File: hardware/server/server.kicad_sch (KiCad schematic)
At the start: 12 parts

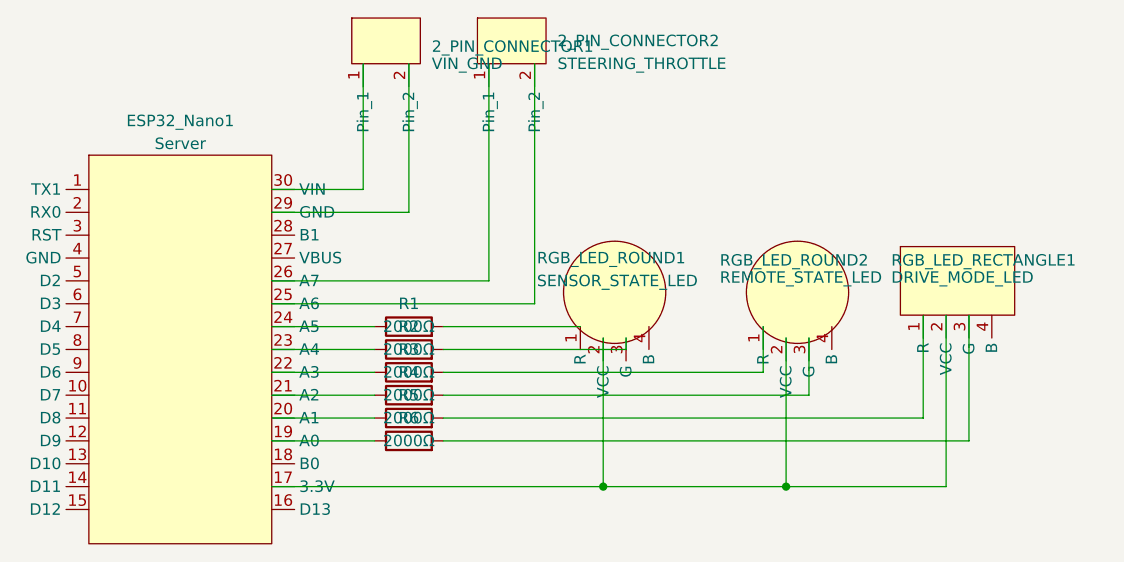
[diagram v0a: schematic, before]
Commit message: hardware: Add more footprint measurement.
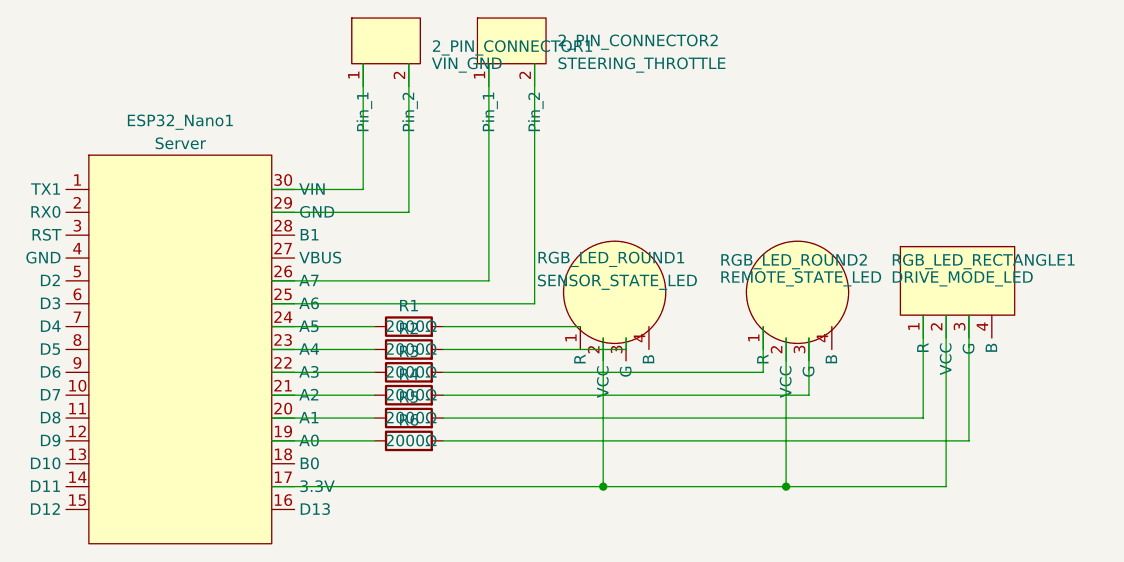
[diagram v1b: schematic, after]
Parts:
- removed R1, R2, R3, R4, R5, R6: 2000Ω, Autocam:Simple Resistor, symbol Device:R
- added R1, R2, R3, R4, R5, R6: 2000Ω, Autocam:Simple Resistor, symbol Autocam:Simple Resistor
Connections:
- net at RGB_LED_ROUND1.1 (R): now also R1.2
- net at RGB_LED_ROUND1.3 (G): now also R2.2
- net at ESP32_Nano1.23 (A4): now also R2.1
- net at ESP32_Nano1.21 (A2): now also R4.1
- net at RGB_LED_ROUND2.3 (G): now also R4.2
- net at ESP32_Nano1.19 (A0): now also R6.1
- net at ESP32_Nano1.20 (A1): now also R5.1
- net at ESP32_Nano1.22 (A3): now also R3.1
- net at ESP32_Nano1.24 (A5): now also R1.1
- net at RGB_LED_ROUND2.1 (R): now also R3.2
- net at RGB_LED_RECTANGLE1.1 (R): now also R5.2
- net at RGB_LED_RECTANGLE1.3 (G): now also R6.2

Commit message: hardware: Add remote PCB.
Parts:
- RGB_LED_RECTANGLE1: value DRIVE_MODE_LED -> DRIVE MODE
- RGB_LED_ROUND1: value SENSOR_STATE_LED -> SENSOR
- RGB_LED_ROUND2: value REMOTE_STATE_LED -> REMOTE
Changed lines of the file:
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@@
 			)
 		)
-		(property "Value" "SENSOR_STATE_LED"
+		(property "Value" "SENSOR"
 			(at 157.734 96.52 0)
 			(effects
@@
 			)
 		)
-		(property "Value" "REMOTE_STATE_LED"
+		(property "Value" "REMOTE"
 			(at 178.054 96.1391 0)
 			(effects
@@
 			)
 		)
-		(property "Value" "DRIVE_MODE_LED"
+		(property "Value" "DRIVE MODE"
 			(at 197.104 96.1391 0)
 			(effects

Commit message: hardware/server: Update LED shape, change to all round LEDs.
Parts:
- removed RGB_LED_RECTANGLE1: DRIVE MODE, Autocam:Anode RGB LED (Rectangle), symbol Autocam:ANODE_RGB_LED_Rectangle
- added RGB_LED_ROUND3: DRIVE_MODE, Autocam:Anode RGB LED (Round), symbol Autocam:ANODE_RGB_LED_Round
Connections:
- net at ESP32_Nano1.17 (3.3V), RGB_LED_ROUND1.2 (VCC), RGB_LED_ROUND2.2 (VCC): now also RGB_LED_ROUND3.2 (VCC)
- net at R6.2: now also RGB_LED_ROUND3.3 (G)
- net at R5.2: now also RGB_LED_ROUND3.1 (R)
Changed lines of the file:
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@@
 	(wire
 		(pts
-			(xy 185.42 119.38) (xy 203.2 119.38)
+			(xy 185.42 119.38) (xy 205.74 119.38)
 		)
 		(stroke
@@
 	(wire
 		(pts
-			(xy 147.32 111.76) (xy 200.66 111.76)
+			(xy 147.32 111.76) (xy 203.2 111.76)
 		)
 		(stroke
@@
 	(wire
 		(pts
-			(xy 205.74 100.33) (xy 205.74 114.3)
+			(xy 208.28 102.87) (xy 208.28 114.3)
 		)
 		(stroke
@@
 	(wire
 		(pts
-			(xy 205.74 114.3) (xy 147.32 114.3)
+			(xy 208.28 114.3) (xy 147.32 114.3)
 		)
 		(stroke
@@
 	(wire
 		(pts
-			(xy 203.2 100.33) (xy 203.2 119.38)
+			(xy 205.74 102.87) (xy 205.74 119.38)
 		)
 		(stroke
@@
 	(wire
 		(pts
-			(xy 200.66 111.76) (xy 200.66 100.33)
+			(xy 203.2 101.6) (xy 203.2 111.76)
 		)
 		(stroke
@@
 	)
 	(symbol
-		(lib_id "Autocam:ANODE_RGB_LED_Rectangle")
-		(at 204.47 97.79 0)
-		(unit 1)
-		(exclude_from_sim no)
-		(in_bom yes)
-		(on_board yes)
-		(dnp no)
-		(property "Reference" "RGB_LED_RECTANGLE1"
-			(at 197.104 94.234 0)
-			(effects
-				(font
-					(size 1.27 1.27)
-				)
-				(justify left)
-			)
-		)
-		(property "Value" "DRIVE MODE"
-			(at 197.104 96.1391 0)
-			(effects
-				(font
-					(size 1.27 1.27)
-				)
-				(justify left)
-			)
-		)
-		(property "Footprint" "Autocam:Anode RGB LED (Rectangle)"
-			(at 195.58 101.6 0)
-			(effects
-				(font
-					(size 1.27 1.27)
-				)
-				(hide yes)
-			)
-		)
-		(property "Datasheet" ""
-			(at 195.58 101.6 0)
-			(effects
-				(font
-					(size 1.27 1.27)
-				)
-				(hide yes)
-			)
-		)
-		(property "Description" ""
-			(at 195.58 101.6 0)
-			(effects
-				(font
-					(size 1.27 1.27)
-				)
-				(hide yes)
-			)
-		)
-		(pin "1"
-		)
-		(pin "2"
-		)
-		(pin "3"
-		)
-		(pin "4"
-		)
-		(instances
-			(project ""
-				(path "/2207becf-5ee2-475e-b366-27d8c790b7c3"
-					(reference "RGB_LED_RECTANGLE1")
-					(unit 1)
-				)
-			)
-		)
-	)
-	(symbol
 		(lib_id "Autocam:Simple Resistor")
 		(at 143.51 106.68 90)
@@
 					(unit 1)
 				)
+			)
+		)
+	)
+	(symbol
+		(lib_id "Autocam:ANODE_RGB_LED_Round")
+		(at 207.01 97.79 0)
+		(unit 1)
+		(exclude_from_sim no)
+		(in_bom yes)
+		(on_board yes)
+		(dnp no)
+		(property "Reference" "RGB_LED_ROUND3"
+			(at 198.374 94.234 0)
+			(effects
+				(font
+					(size 1.27 1.27)
+				)
+				(justify left)
+			)
+		)
+		(property "Value" "DRIVE_MODE"
+			(at 198.374 96.1391 0)
+			(effects
+				(font
+					(size 1.27 1.27)
+				)
+				(justify left)
+			)
+		)
+		(property "Footprint" "Autocam:Anode RGB LED (Round)"
+			(at 198.12 102.87 0)
+			(effects
+				(font
+					(size 1.27 1.27)
+				)
+				(hide yes)
+			)
+		)
+		(property "Datasheet" ""
+			(at 198.12 102.87 0)
+			(effects
+				(font
+					(size 1.27 1.27)
+				)
+				(hide yes)
+			)
+		)
+		(property "Description" ""
+			(at 198.12 102.87 0)
+			(effects
+				(font
+					(size 1.27 1.27)
+				)
+				(hide yes)
+			)
+		)
+		(pin "1"
+		)
+		(pin "2"
+		)
+		(pin "3"
+		)
+		(pin "4"
+		)
+		(instances
+			(project "server"
+				(path "/2207becf-5ee2-475e-b366-27d8c790b7c3"
+					(reference "RGB_LED_ROUND3")
+					(unit 1)
+				)

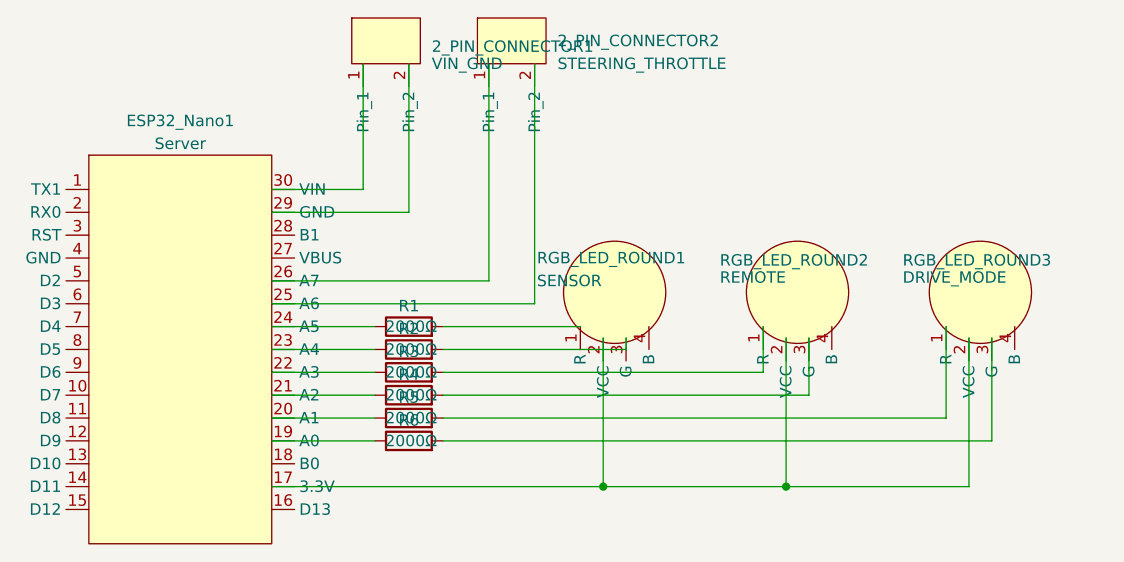
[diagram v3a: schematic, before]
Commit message: hardware: Increase the LED resistor from 2000Ω to 10KΩ.
To reduce the power consumption.
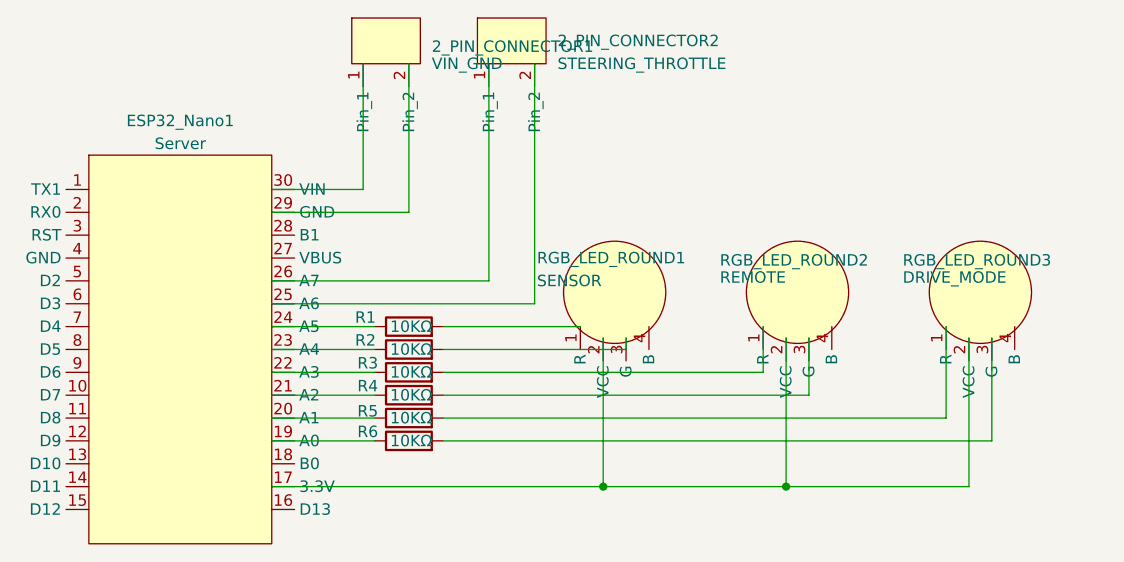
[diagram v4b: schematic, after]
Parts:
- R1, R2, R3, R4, R5, R6: value 2000Ω -> 10KΩ
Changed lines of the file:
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@@
 		(dnp no)
 		(property "Reference" "R1"
-			(at 143.51 99.314 90)
-			(effects
-				(font
-					(size 1.27 1.27)
-				)
-			)
-		)
-		(property "Value" "2000Ω"
+			(at 138.684 100.584 90)
+			(effects
+				(font
+					(size 1.27 1.27)
+				)
+			)
+		)
+		(property "Value" "10KΩ"
 			(at 143.764 101.6 90)
 			(effects
@@
 		(dnp no)
 		(property "Reference" "R6"
-			(at 143.51 112.014 90)
-			(effects
-				(font
-					(size 1.27 1.27)
-				)
-			)
-		)
-		(property "Value" "2000Ω"
+			(at 138.938 113.284 90)
+			(effects
+				(font
+					(size 1.27 1.27)
+				)
+			)
+		)
+		(property "Value" "10KΩ"
 			(at 143.764 114.3 90)
 			(effects
@@
 		(dnp no)
 		(property "Reference" "R2"
-			(at 143.51 101.854 90)
-			(effects
-				(font
-					(size 1.27 1.27)
-				)
-			)
-		)
-		(property "Value" "2000Ω"
+			(at 138.684 103.124 90)
+			(effects
+				(font
+					(size 1.27 1.27)
+				)
+			)
+		)
+		(property "Value" "10KΩ"
 			(at 143.764 104.14 90)
 			(effects
@@
 		(dnp no)
 		(property "Reference" "R4"
-			(at 143.51 106.934 90)
-			(effects
-				(font
-					(size 1.27 1.27)
-				)
-			)
-		)
-		(property "Value" "2000Ω"
+			(at 138.938 108.204 90)
+			(effects
+				(font
+					(size 1.27 1.27)
+				)
+			)
+		)
+		(property "Value" "10KΩ"
 			(at 143.764 109.22 90)
 			(effects
@@
 		(dnp no)
 		(property "Reference" "R3"
-			(at 143.51 104.394 90)
-			(effects
-				(font
-					(size 1.27 1.27)
-				)
-			)
-		)
-		(property "Value" "2000Ω"
+			(at 138.938 105.664 90)
+			(effects
+				(font
+					(size 1.27 1.27)
+				)
+			)
+		)
+		(property "Value" "10KΩ"
 			(at 143.764 106.68 90)
 			(effects
@@
 		(dnp no)
 		(property "Reference" "R5"
-			(at 143.51 109.474 90)
-			(effects
-				(font
-					(size 1.27 1.27)
-				)
-			)
-		)
-		(property "Value" "2000Ω"
+			(at 138.938 110.998 90)
+			(effects
+				(font
+					(size 1.27 1.27)
+				)
+			)
+		)
+		(property "Value" "10KΩ"
 			(at 143.764 111.76 90)
 			(effects

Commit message: hardware: Reroute the wires to fix unavailable PINs.
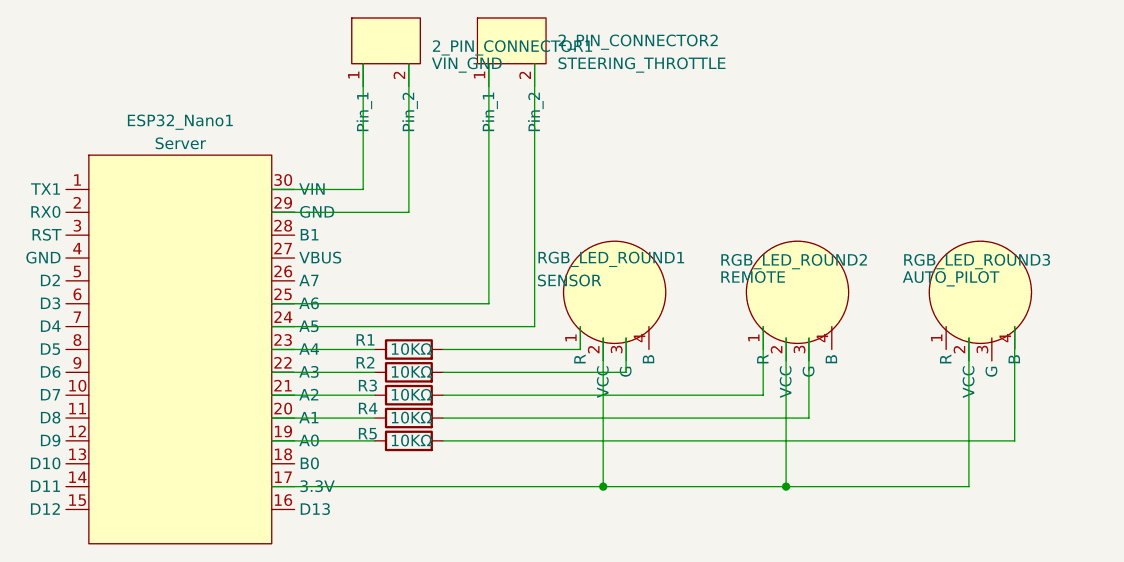
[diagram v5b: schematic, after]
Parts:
- removed R6: 10KΩ, Autocam:Simple Resistor, symbol Autocam:Simple Resistor
- RGB_LED_ROUND3: value DRIVE_MODE -> AUTO_PILOT
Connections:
- net at ESP32_Nano1.19 (A0): now also R5.1
- net at ESP32_Nano1.20 (A1): now also R4.1; no longer R5.1
- net at ESP32_Nano1.21 (A2): now also R3.1; no longer R4.1
- net at ESP32_Nano1.22 (A3): now also R2.1; no longer R3.1
- net at ESP32_Nano1.23 (A4): now also R1.1; no longer R2.1
- net at ESP32_Nano1.24 (A5): now also 2_PIN_CONNECTOR2.2 (Pin_2); no longer R1.1
- net at ESP32_Nano1.25 (A6): now also 2_PIN_CONNECTOR2.1 (Pin_1); no longer 2_PIN_CONNECTOR2.2 (Pin_2)
- net at ESP32_Nano1.26 (A7): no longer 2_PIN_CONNECTOR2.1 (Pin_1)
- net at R5.2: now also RGB_LED_ROUND3.4 (B); no longer RGB_LED_ROUND3.1 (R)
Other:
- moved on the sheet: R1, R2, R3, R4, R5

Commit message: hardware: Revise the drive mode naming.
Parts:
- RGB_LED_ROUND3: value AUTO_PILOT -> DRIVE_MODE
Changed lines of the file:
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@@
 			)
 		)
-		(property "Value" "AUTO_PILOT"
+		(property "Value" "DRIVE_MODE"
 			(at 198.374 96.1391 0)
 			(effects
